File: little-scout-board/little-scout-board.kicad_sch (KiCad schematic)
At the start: 8 parts, among them J1 AP63203, J2 TMP36, J3 USB_B_Mini, J4 M1_Terminal, J5 M2_Terminal, U1 ESP32-DevKitC

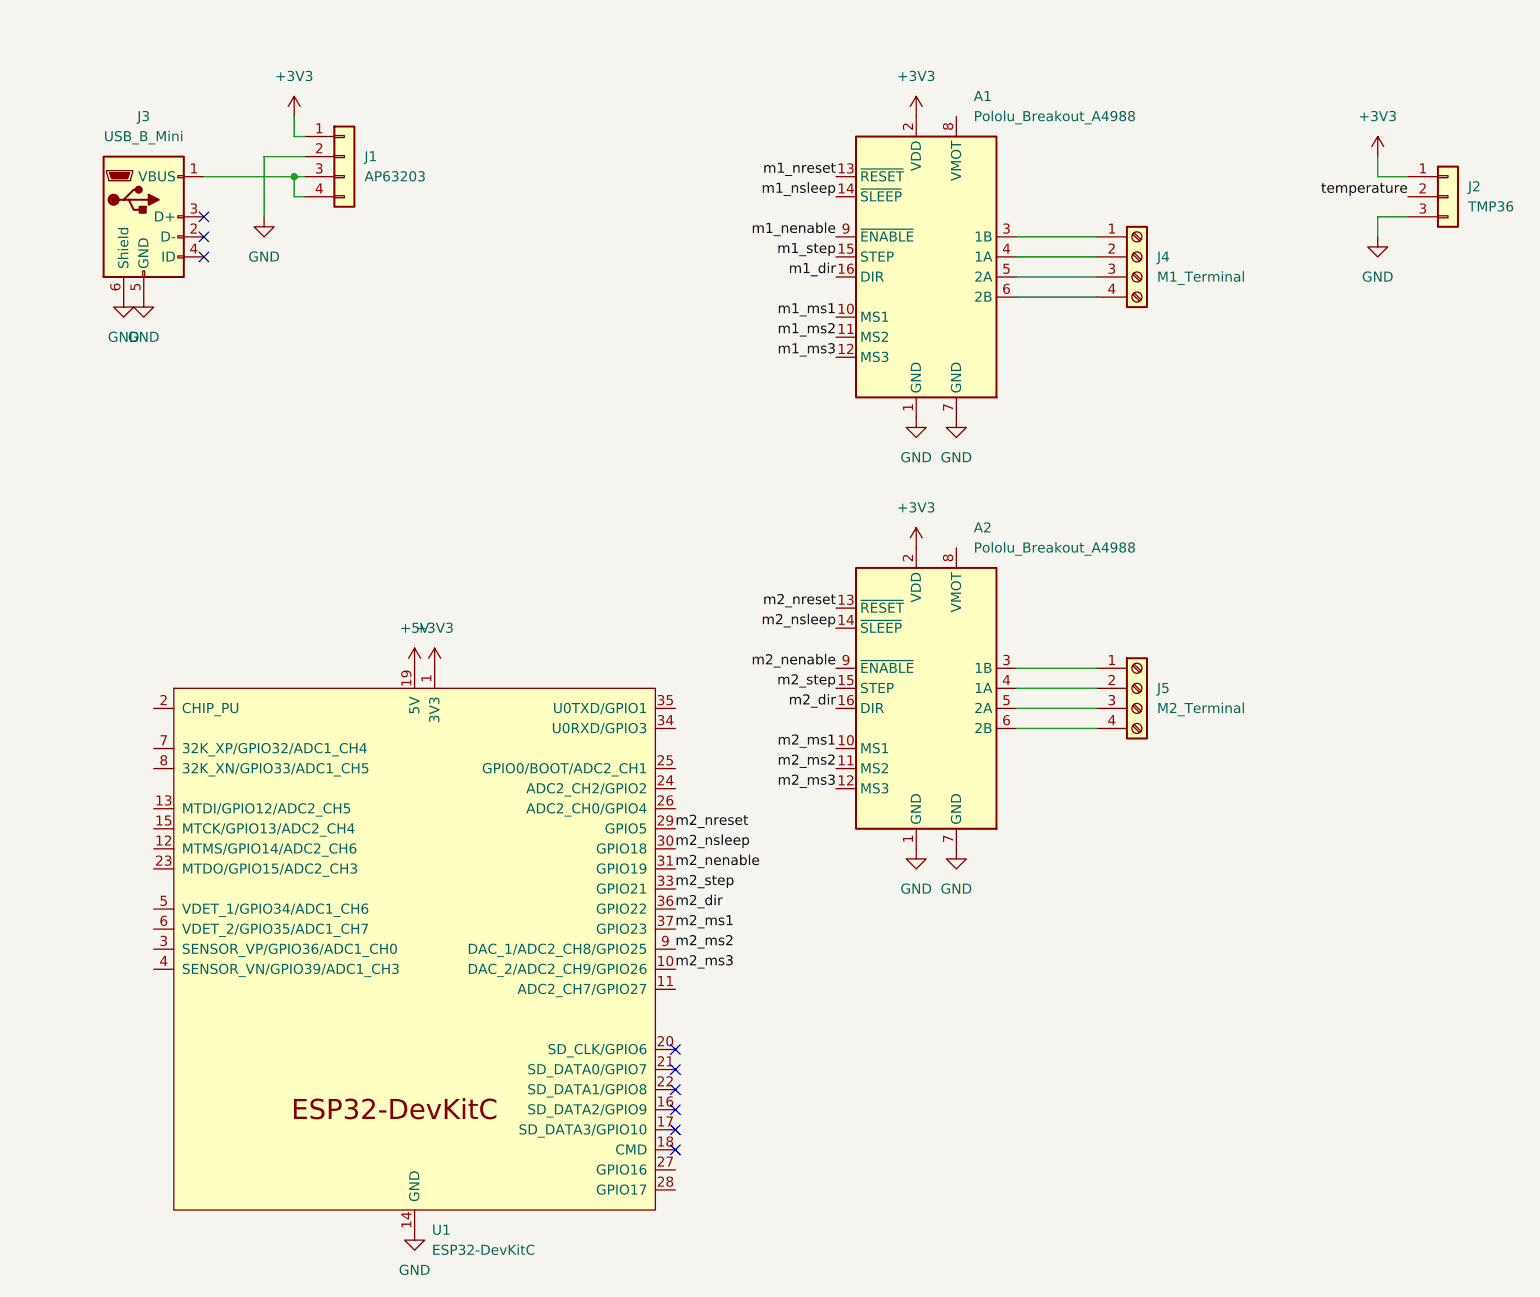
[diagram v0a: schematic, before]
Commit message: change power in to screw terminal
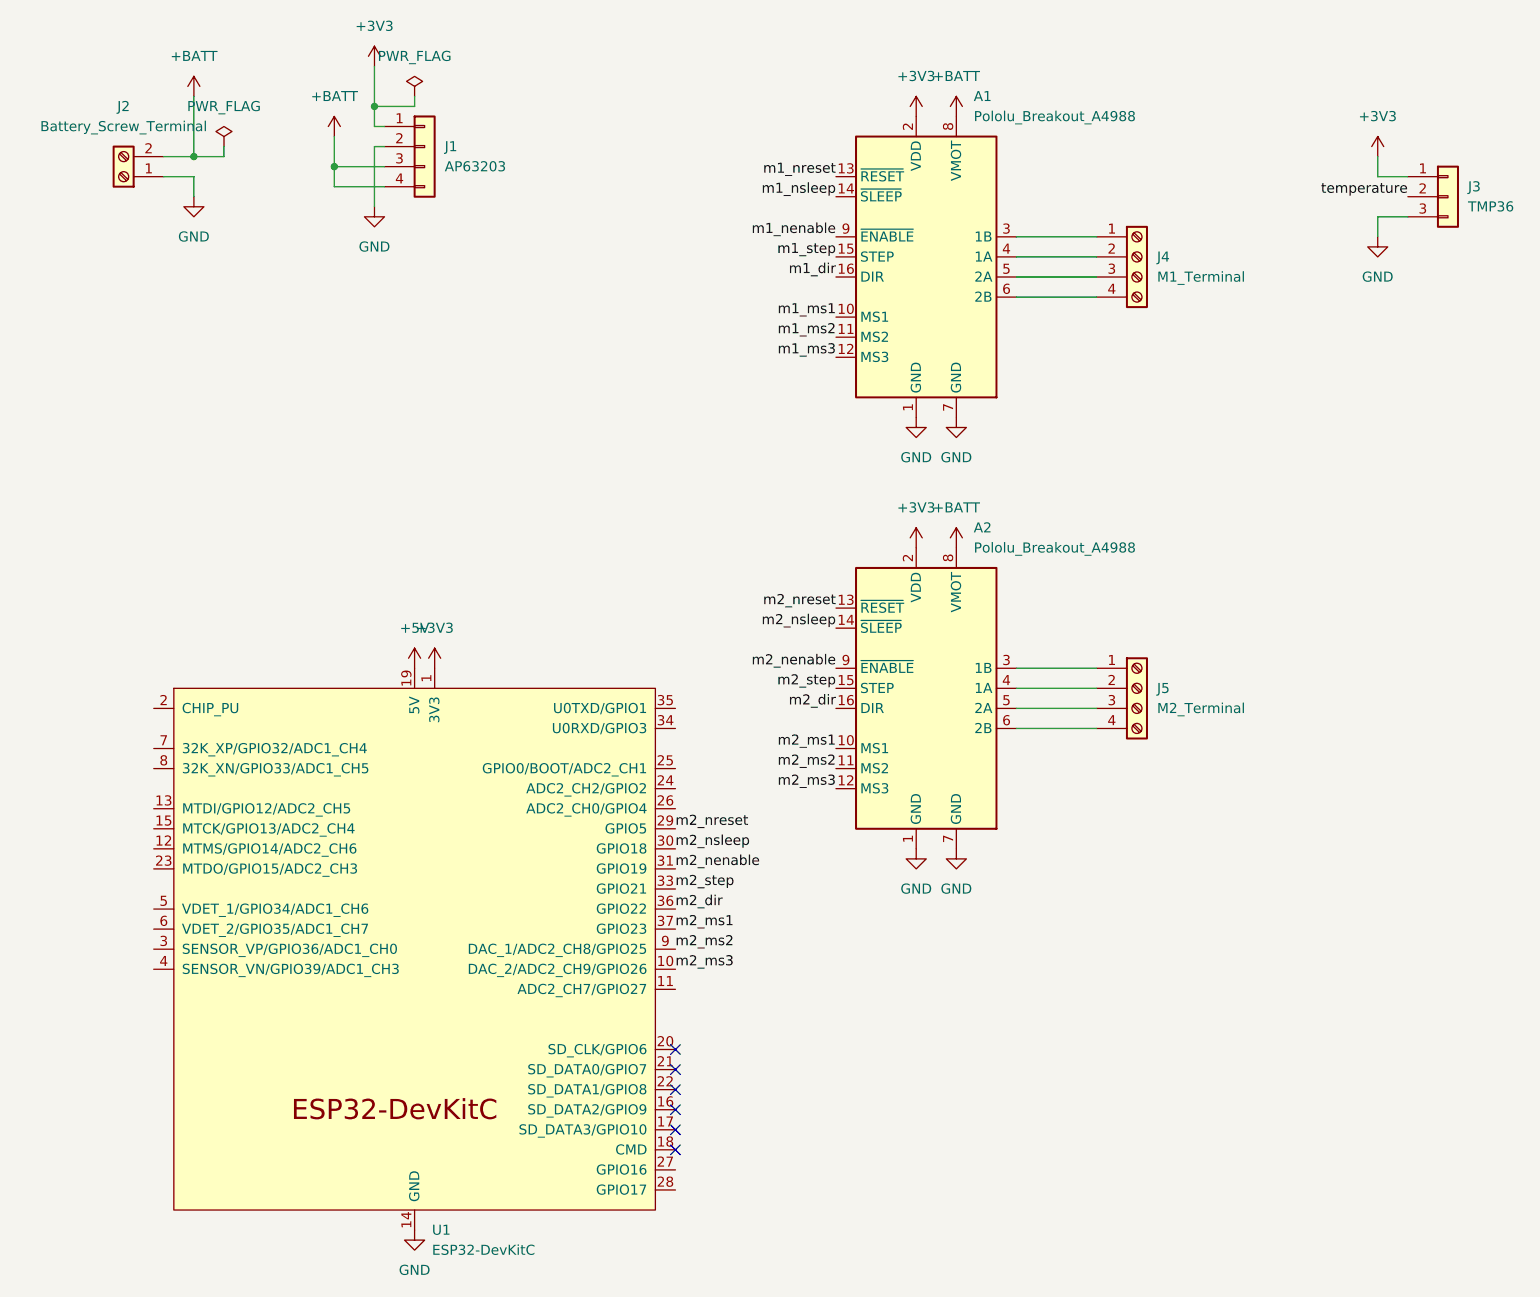
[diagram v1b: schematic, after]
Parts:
- removed J3: USB_B_Mini, symbol Connector:USB_B_Mini
- added J2: Battery_Screw_Terminal, symbol Connector:Screw_Terminal_01x02
- renumbered J2 to J3
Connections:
- net GND: now also J2.1 (Pin_1)
- net +BATT: now reaches A1.8 (VMOT)
- net +BATT: now also A2.8 (VMOT), J1.3 (Pin_3), J1.4 (Pin_4), J2.2 (Pin_2)
- no-connect marks 9 -> 6
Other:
- moved on the sheet: J1
